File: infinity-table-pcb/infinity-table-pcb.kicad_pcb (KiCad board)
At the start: 2 copper layers, 87.6 x 34.8 mm, 15 parts, among them J1 PJ-063AH, J2 Conn_01x04_Male, J3 Conn_01x10_Male, SW1 SW_Push_Dual, SW2 SW_Push_Dual, U1 TXS0108EPW

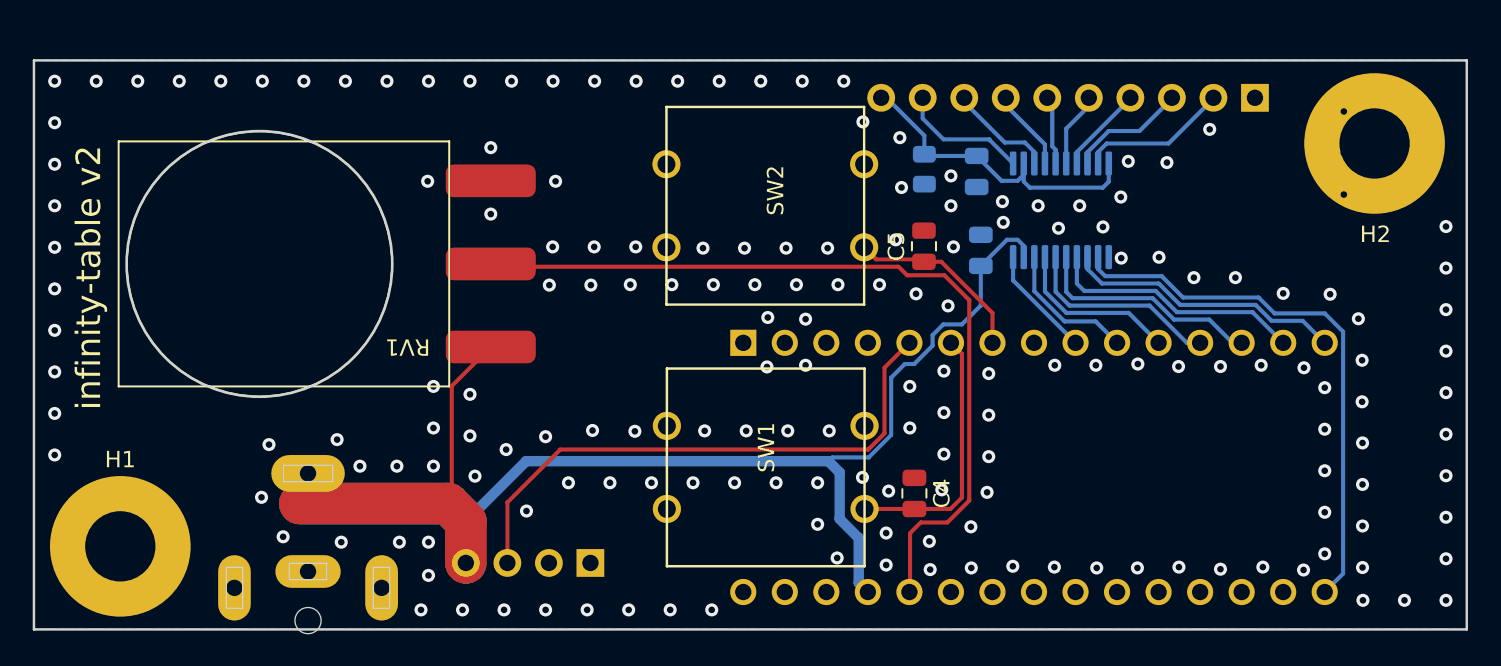
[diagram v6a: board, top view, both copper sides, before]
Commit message: holes and texts
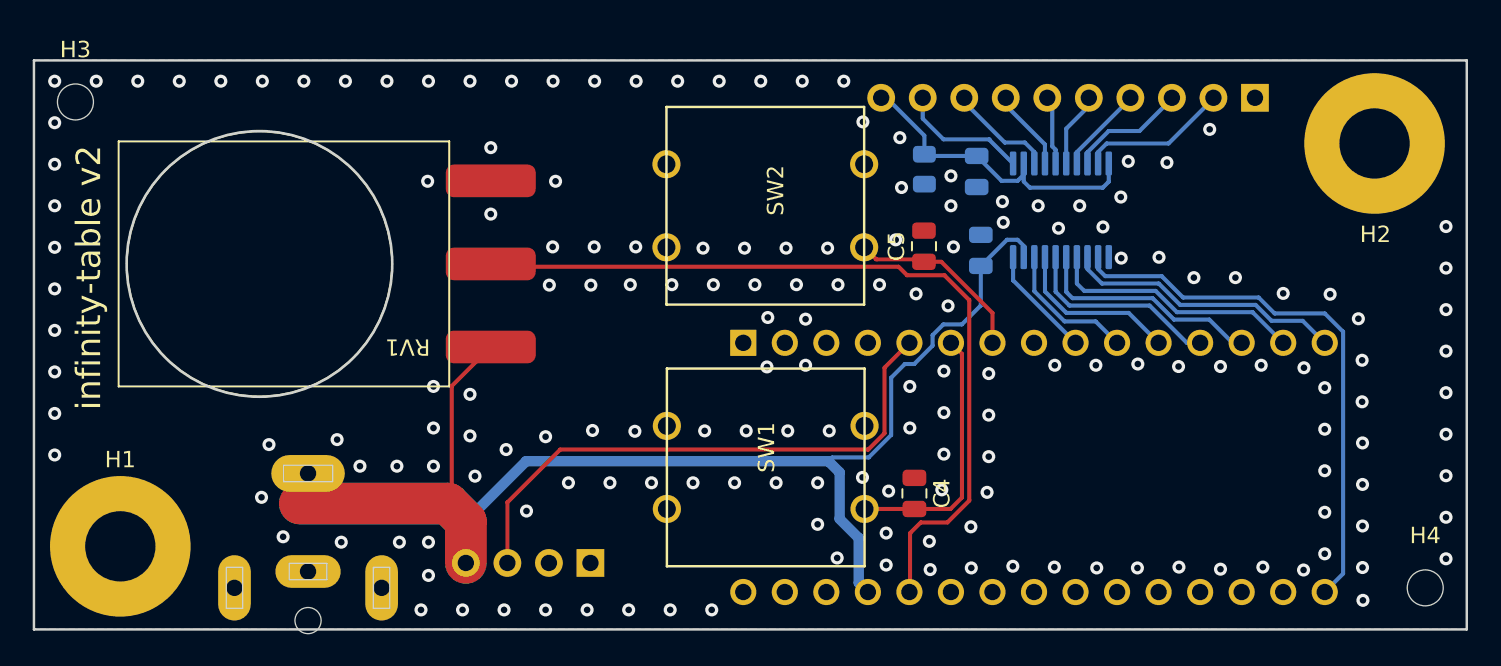
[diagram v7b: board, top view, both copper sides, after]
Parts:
- added H3: MountingHole, MountingHole:MountingHole_2.2mm_M2, F.Cu at (68.6, 81.3)
- added H4: MountingHole, MountingHole:MountingHole_2.2mm_M2, F.Cu at (151.1, 111.0)
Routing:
- net GND: vias 180 -> 175
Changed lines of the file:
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@@
   (net 39 "unconnected-(SW1-Pad1)")
   (net 40 "unconnected-(SW2-Pad1)")
+  (footprint "MountingHole:MountingHole_2.2mm_M2" (layer "F.Cu")
+    (at 151.13 110.998)
+    (descr "Mounting Hole 2.2mm, no annular, M2")
+    (tags "mounting hole 2.2mm no annular m2")
+    (property "Sheetfile" "infinity-table-pcb.kicad_sch")
+    (property "Sheetname" "")
+    (attr exclude_from_pos_files)
+    (fp_text reference "H4" (at 0 -3.2) (layer "F.SilkS")
+      (effects (font (size 1 1) (thickness 0.15)))
+    )
+    (fp_text value "MountingHole" (at 0 3.2) (layer "F.Fab")
+      (effects (font (size 1 1) (thickness 0.15)))
+    )
+    (fp_text user "${REFERENCE}" (at 0.3 0) (layer "F.Fab")
+      (effects (font (size 1 1) (thickness 0.15)))
+    )
+    (fp_circle (center 0 0) (end 2.2 0) (layer "Cmts.User") (width 0.15) (fill none))
+    (fp_circle (center 0 0) (end 2.45 0) (layer "F.CrtYd") (width 0.05) (fill none))
+    (pad "" np_thru_hole circle (at 0 0) (size 2.2 2.2) (drill 2.2) (layers *.Cu *.Mask))
+  )
   (footprint "MountingHole:MountingHole_4.3mm_M4_Pad" (layer "F.Cu")
     (at 71.3232 108.458)
@@
     (pad "3" connect roundrect (at -5.08 10.16 180) (size 5.5 2) (layers "F.Cu" "F.Mask") (roundrect_rratio 0.25)
       (net 1 "GND") (pinfunction "3") (pintype "passive"))
+  )
+  (footprint "MountingHole:MountingHole_2.2mm_M2" (layer "F.Cu")
+    (at 68.58 81.28)
+    (descr "Mounting Hole 2.2mm, no annular, M2")
+    (tags "mounting hole 2.2mm no annular m2")
+    (property "Sheetfile" "infinity-table-pcb.kicad_sch")
+    (property "Sheetname" "")
+    (attr exclude_from_pos_files)
+    (fp_text reference "H3" (at 0 -3.2) (layer "F.SilkS")
+      (effects (font (size 1 1) (thickness 0.15)))
+    )
+    (fp_text value "MountingHole" (at 0 3.2) (layer "F.Fab")
+      (effects (font (size 1 1) (thickness 0.15)))
+    )
+    (fp_text user "${REFERENCE}" (at 0.3 0) (layer "F.Fab")
+      (effects (font (size 1 1) (thickness 0.15)))
+    )
+    (fp_circle (center 0 0) (end 2.2 0) (layer "Cmts.User") (width 0.15) (fill none))
+    (fp_circle (center 0 0) (end 2.45 0) (layer "F.CrtYd") (width 0.05) (fill none))
+    (pad "" np_thru_hole circle (at 0 0) (size 2.2 2.2) (drill 2.2) (layers *.Cu *.Mask))
   )
   (footprint "kicad-ss-libs:Push Button 12x12mm" (layer "F.Cu")
@@
   (gr_circle (center 79.8322 91.186) (end 79.883 99.314) (layer "Edge.Cuts") (width 0.15) (fill none))
   (gr_line (start 153.67 113.538) (end 66.04 113.538) (layer "Edge.Cuts") (width 0.15))
-  (gr_text "Sami Sorell" (at 96.7486 95.9866 150) (layer "B.SilkS")
-    (effects (font (size 1.5 1.5) (thickness 0.3)) (justify mirror))
+  (gr_text "Sami\nSorell" (at 95.5802 91.6178 90) (layer "B.SilkS")
+    (effects (font (size 5 5) (thickness 1)) (justify mirror))
   )
   (gr_text "infinity-table v2" (at 69.3928 92.0242 90) (layer "B.SilkS")
@@
     (effects (font (size 1.5 1.5) (thickness 0.3)))
   )
-  (via (at 149.86 111.76) (size 0.8) (drill 0.4) (layers "F.Cu" "B.Cu") (free) (net 1))
   (via (at 132.5372 90.8304) (size 0.8) (drill 0.4) (layers "F.Cu" "B.Cu") (free) (net 1))
   (via (at 135.3312 84.9884) (size 0.8) (drill 0.4) (layers "F.Cu" "B.Cu") (free) (net 1))
@@
   (via (at 122.1232 87.63) (size 0.8) (drill 0.4) (layers "F.Cu" "B.Cu") (free) (net 1))
   (via (at 121.6914 97.7392) (size 0.8) (drill 0.4) (layers "F.Cu" "B.Cu") (free) (net 1))
-  (via (at 146.1516 84.4042) (size 0.8) (drill 0.4) (layers "F.Cu" "B.Cu") (free) (net 1))
   (via (at 85.979 103.5558) (size 0.8) (drill 0.4) (layers "F.Cu" "B.Cu") (free) (net 1))
   (via (at 100.203 101.3714) (size 0.8) (drill 0.4) (layers "F.Cu" "B.Cu") (free) (net 1))
@@
   (via (at 117.7544 92.456) (size 0.8) (drill 0.4) (layers "F.Cu" "B.Cu") (free) (net 1))
   (via (at 152.4 101.6) (size 0.8) (drill 0.4) (layers "F.Cu" "B.Cu") (free) (net 1))
-  (via (at 146.1516 81.8642) (size 0.8) (drill 0.4) (layers "F.Cu" "B.Cu") (free) (net 1))
   (via (at 107.061 101.3968) (size 0.8) (drill 0.4) (layers "F.Cu" "B.Cu") (free) (net 1))
   (via (at 139.5222 92.0242) (size 0.8) (drill 0.4) (layers "F.Cu" "B.Cu") (free) (net 1))
@@
   (via (at 102.4128 112.3442) (size 0.8) (drill 0.4) (layers "F.Cu" "B.Cu") (free) (net 1))
   (via (at 112.141 101.3968) (size 0.8) (drill 0.4) (layers "F.Cu" "B.Cu") (free) (net 1))
-  (via (at 152.4 111.76) (size 0.8) (drill 0.4) (layers "F.Cu" "B.Cu") (free) (net 1))
   (via (at 147.2946 109.7534) (size 0.8) (drill 0.4) (layers "F.Cu" "B.Cu") (free) (net 1))
   (via (at 119.6086 98.679) (size 0.8) (drill 0.4) (layers "F.Cu" "B.Cu") (free) (net 1))
@@
   (via (at 102.7938 101.4222) (size 0.8) (drill 0.4) (layers "F.Cu" "B.Cu") (free) (net 1))
   (via (at 113.2332 97.3836) (size 0.8) (drill 0.4) (layers "F.Cu" "B.Cu") (free) (net 1))
-  (via (at 146.1516 86.9442) (size 0.8) (drill 0.4) (layers "F.Cu" "B.Cu") (free) (net 1))
   (via (at 67.31 100.33) (size 0.8) (drill 0.4) (layers "F.Cu" "B.Cu") (free) (net 1))
   (via (at 89.7128 112.3442) (size 0.8) (drill 0.4) (layers "F.Cu" "B.Cu") (free) (net 1))
